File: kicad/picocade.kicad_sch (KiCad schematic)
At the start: 9 parts, among them SW1 SW_Push, SW2 SW_Push, SW3 SW_Push, SW4 SW_Push, SW5 SW_Push, SW6 SW_Push, SW7 SW_Push, SW8 SW_Push, U1 PicoW

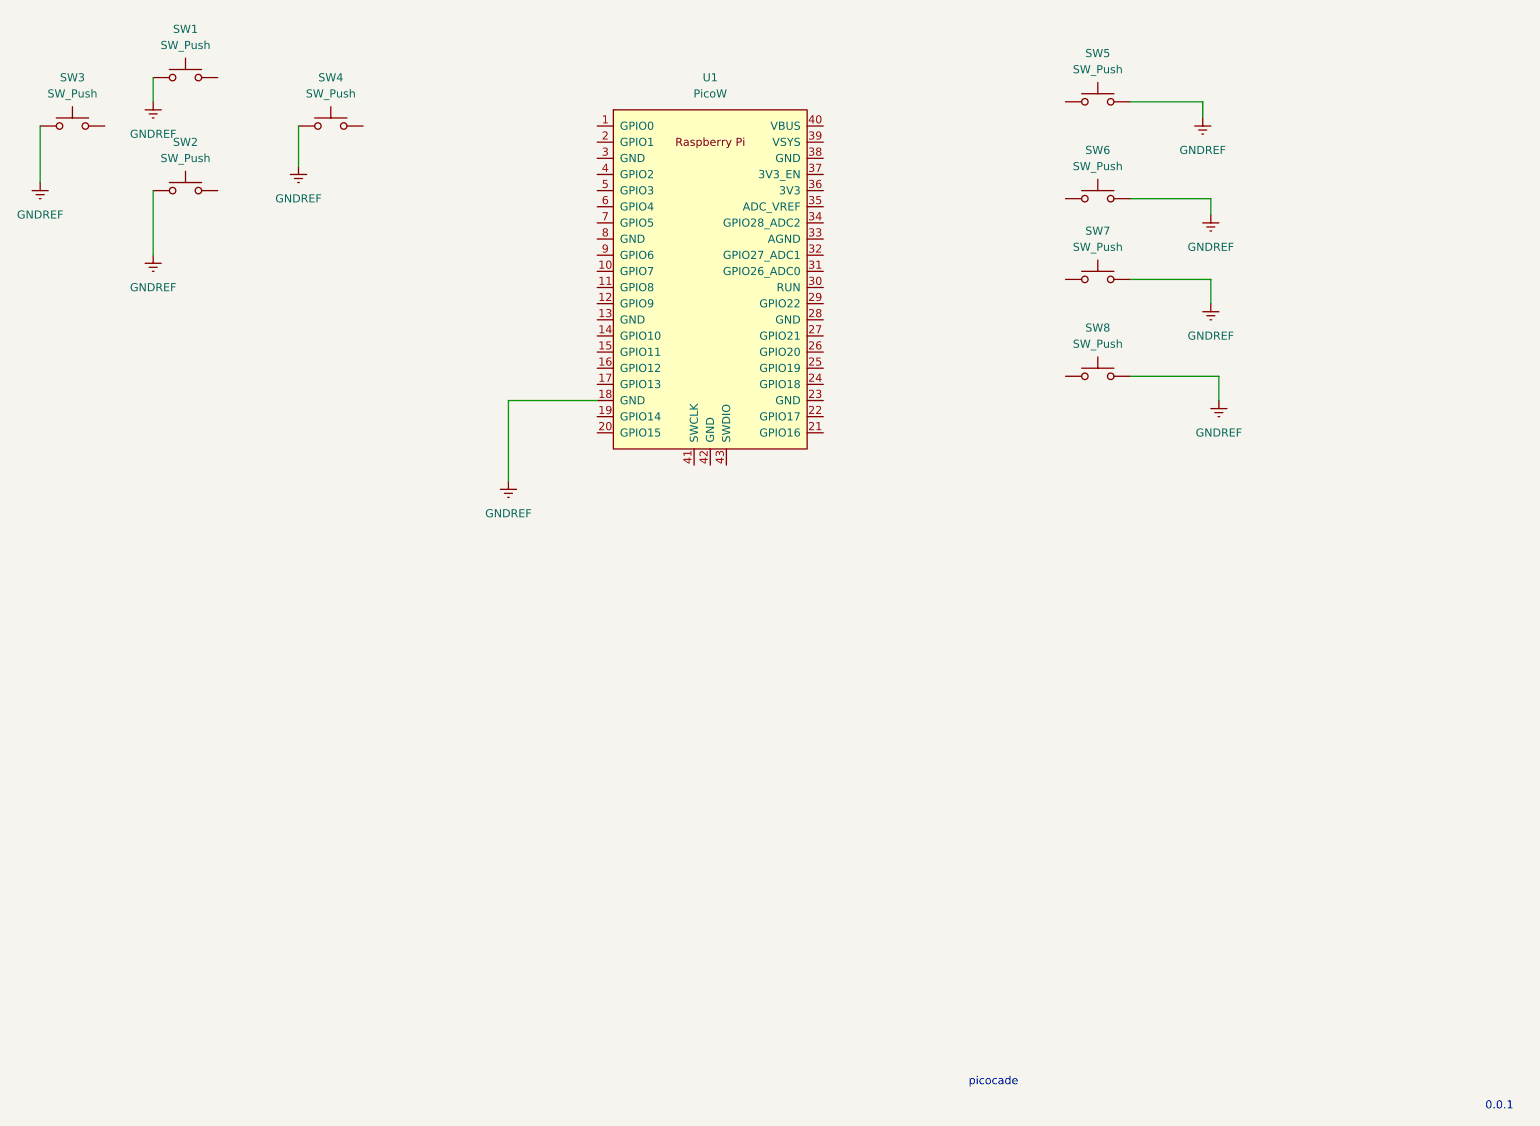
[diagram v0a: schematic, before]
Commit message: add swithces to schematics
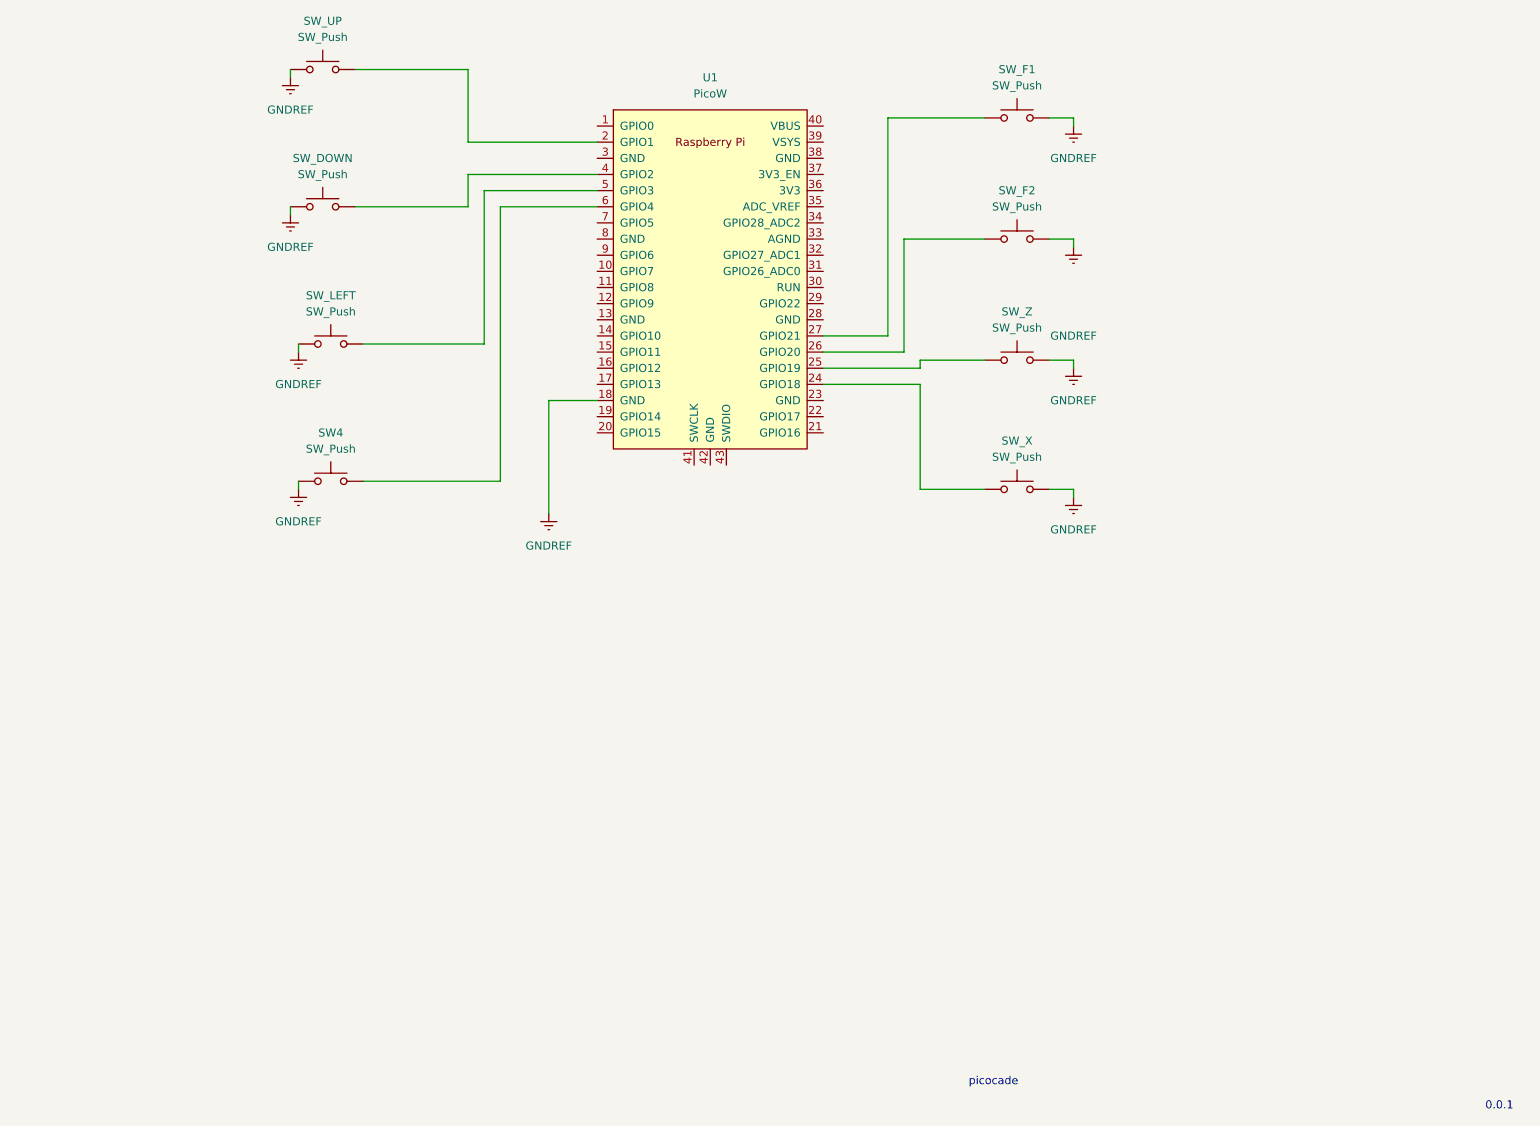
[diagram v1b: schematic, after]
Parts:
- renumbered SW2 to SW_DOWN, SW5 to SW_F1, SW6 to SW_F2, SW3 to SW_LEFT, SW1 to SW_UP, SW8 to SW_X, SW7 to SW_Z
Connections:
- net at SW_F2.1: now also U1.26 (GPIO20)
- net at SW_X.1: now also U1.24 (GPIO18)
- net at U1.2 (GPIO1): now also SW_UP.2
- net at U1.25 (GPIO19): now also SW_Z.1
- net at U1.27 (GPIO21): now also SW_F1.1
- net at U1.4 (GPIO2): now also SW_DOWN.2
- net at U1.5 (GPIO3): now also SW_LEFT.2
- net at U1.6 (GPIO4): now also SW4.2
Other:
- moved on the sheet: SW4, SW_DOWN, SW_F1, SW_F2, SW_LEFT, SW_UP, SW_X, SW_Z
